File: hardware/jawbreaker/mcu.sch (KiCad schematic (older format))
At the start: 122 parts, among them J1 GSG-USB-MICRO-B, P1 ANALOG, P10 BANK1_AUX, P11 SPIFI, P12 SD, P14 LPC_ISP, P15 I2S, P16 1V8, P17 VCC, P18 CPLD_JTAG, P2 LPC_JTAG, P3 LPC_MISC, P5 GPIO, P8 BANK2_AUX, U1 GSG-IP4220CZ6, U2 LPC43XXFBD144, U3 W25Q80BV, U4 GSG-XC2C64A-7VQG100C, U5 TPS62410

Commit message: re-annotated everything
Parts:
- gave numbers to parts that had none: 26
- renumbered C24 to C125, C27 to C126, C30 to C127, C1 to C128, C2 to C129, C3 to C130, C4 to C131, C5 to C132, C7 to C133, C9 to C134, C10 to C135, C11 to C136, C12 to C137, C13 to C138, C14 to C139, C15 to C140, C17 to C141, C19 to C142, C21 to C143, C20 to C144, C28 to C145, C31 to C146, C6 to C147, C8 to C148, C22 to C149, C23 to C150, C25 to C151, C26 to C152, C29 to C153, C32 to C154, C33 to C155, C16 to C156, C18 to C159, D6 to D2, D7 to D3, D1 to D4, D2 to D5, D3 to D6, D4 to D7, D5 to D8, L1 to L10, L2 to L11, P11 to P19, P5 to P20, P1 to P21, P15 to P22, P17 to P23, P16 to P24, P14 to P25, P2 to P26, P3 to P27, P12 to P28, P18 to P29, P8 to P30, P10 to P31, R35 to R46, R37 to R47, R16 to R48, R17 to R49, R33 to R50, R32 to R51, R39 to R52, R34 to R53, R40 to R54, R36 to R55, R38 to R56, R1 to R57, R2 to R58, R28 to R59, R10 to R62, R30 to R63, R31 to R64, R11 to R65, R5 to R66, R6 to R67, R7 to R68, R14 to R69, R29 to R70, R3 to R71, R8 to R72, R9 to R73, R12 to R74, R13 to R75, R15 to R76, R18 to R77, R4 to R82, R41 to R93, R42 to R94, R43 to R95, U3 to U20, U5 to U21, U1 to U22, U2 to U23, U4 to U24

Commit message: started replacing 0603s with 0402s
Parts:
- removed C159: 47pF, symbol C
- removed R94, R95: 10k, symbol R
- C125: Description CAP CER 22PF 50V 5% NP0 0603 -> (none); Manufacturer Murata -> (none); Part Number GRM1885C1H220JA01D -> (none)
- C128, C129, C130, C131, C132, C133, C134, C135, C136, C137, C138, C139, C140, C141, C142, C144, C148, C149, C150, C151, C152, C153, C154: Description CAP CER 0.1UF 16V 10% X7R 0603 -> CAP CER 0.1UF 10V 10% X5R 0402; Part Number GRM188R71C104KA01D -> GRM155R61A104KA01D
- C147: value 4u7 -> 100nF; Description CAP CER 4.7UF 10V 10% X5R 0805 -> CAP CER 0.1UF 10V 10% X5R 0402; Manufacturer Taiyo Yuden -> Murata; Part Number LMK212BJ475KD-T -> GRM155R61A104KA01D
- C155: value 100nF -> 100pF; Description CAP CER 0.1UF 16V 10% X7R 0603 -> CAP CER 100PF 50V 5% NP0 0402; Part Number GRM188R71C104KA01D -> GRM1555C1H101JZ01D
- C156: value 100pF -> 47pF; Description CAP CER 100PF 50V 5% NP0 0603 -> CAP CER 47PF 50V 5% NP0 0402; Part Number GRM1885C1H101JA01D -> GRM1555C1H470JZ01D
- R46: Description RES 180K OHM 1/10W 1% 0603 SMD -> (none); Manufacturer Panasonic -> (none); Part Number ERJ-3EKF1803V -> (none)
- R47: Description RES 360K OHM 1/10W 1% 0603 SMD -> (none); Manufacturer Panasonic -> (none); Part Number ERJ-3EKF3603V -> (none)
- R48, R49, R51, R52, R54, R59, R60, R61, R66, R67, R68, R82, R93: Description RES 10K OHM 1/10W 5% 0603 SMD -> (none); Manufacturer Panasonic -> (none); Part Number ERJ-3GEYJ103V -> (none)
- R55: Description RES 160K OHM 1/10W 1% 0603 SMD -> (none); Manufacturer Panasonic -> (none); Part Number ERJ-3EKF1603V -> (none)
- R56: Description RES 560K OHM 1/10W 1% 0603 SMD -> (none); Manufacturer Panasonic -> (none); Part Number ERJ-3EKF5603V -> (none)
- R57, R58: Description RES 0.0 OHM 1/10W 0603 SMD -> (none); Manufacturer Panasonic -> (none); Part Number ERJ-3GEY0R00V -> (none)
- R62: Description RES 15K OHM 1/10W 5% 0603 SMD -> (none); Manufacturer Panasonic -> (none); Part Number ERJ-3GEYJ153V -> (none)
- R63, R64: value 1k8 -> 10k; Description RES 1.8K OHM 1/10W 5% 0603 SMD -> (none); Manufacturer Panasonic -> (none); Part Number ERJ-3GEYJ182V -> (none)
- R65: Description RES 33K OHM 1/10W 5% 0603 SMD -> (none); Manufacturer Panasonic -> (none); Part Number ERJ-3GEYJ333V -> (none)
- R69: Description RES 12.0K OHM 1/10W 1% 0603 SMD -> (none); Manufacturer Panasonic -> (none); Part Number ERJ-3EKF1202V -> (none)
- R70, R71, R72, R73, R74, R75, R76: Description RES 470 OHM 1/10W 5% 0603 SMD -> RES TF 1/16W 470 OHM 5% 0402; Manufacturer Panasonic -> Stackpole; Part Number ERJ-3GEYJ471V -> RMCF0402JT470R
- R83, R84, R85, R92: value DNP -> 10k; Description RES 10K OHM 1/10W 5% 0603 SMD -> (none); Manufacturer Panasonic -> (none); Part Number ERJ-3GEYJ103V -> (none)
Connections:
- net +1.8V: now also C151.1; no longer C153.1
- net BOOT0: now also R67.1; no longer R82.1
- net BOOT1: now also R68.2; no longer R93.2
- net BOOT2: now also R82.2
- net BOOT3: now also R93.2
- net DBGEN: now also R64.1; no longer R67.2
- net EN1V8: now also R76.2; no longer R76.1
- net GND: now also C156.2, R68.1, R70.1, R71.1, R82.1; no longer C155.2, R70.2, R71.2
- net GP_CLKIN: now also C155.2, C156.1; no longer C156.2
- net ISP: now also R59.1; no longer R59.2
- net LED1: now also R72.2; no longer R72.1
- net LED2: now also R73.2; no longer R73.1
- net LED3: now also R74.2; no longer R74.1
- net LPC_CLK: now also C155.1; no longer C156.1
- net RESET: now also R49.1; no longer R49.2
- net SCL: no longer R64.2
- net SDA: no longer R63.2
- net TCK: now also R66.1; no longer R68.2
- net TDO: now also R63.1; no longer R66.2
- net VBUS: no longer C148.1
- net VCC: now also C148.1, R48.2, R49.2, R59.2, R63.2, R64.2, R66.2, R67.2, R75.2; no longer C151.1, R48.1, R49.1, R59.1, R63.1, R64.1, R66.1, R67.1, R68.1, R75.1, R82.2
- net VCCIO1: now also C153.1; no longer C155.1
- net WAKEUP: now also R48.1; no longer R48.2
- net at D2.2 (K): now also R70.2; no longer R70.1
- net at D6.1 (A): now also R74.1; no longer R74.2
- net at D7.1 (A): now also R75.1; no longer R75.2
- net at D4.1 (A): now also R72.1; no longer R72.2
- net at D8.1 (A): now also R76.1; no longer R76.2
- net at D5.1 (A): now also R73.1; no longer R73.2
- net at D3.2 (K): now also R71.2; no longer R71.1

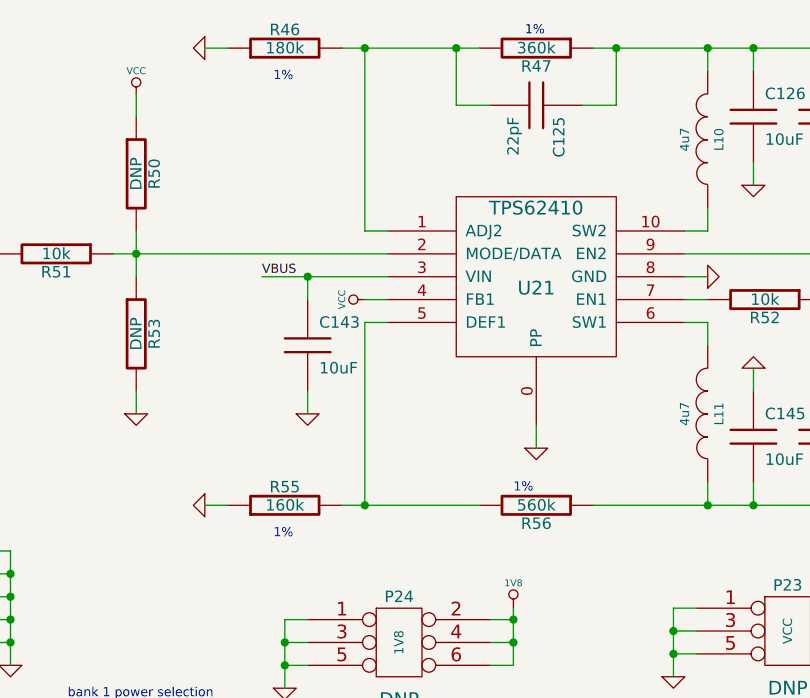
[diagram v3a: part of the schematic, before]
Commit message: updated regulator feedback resistors
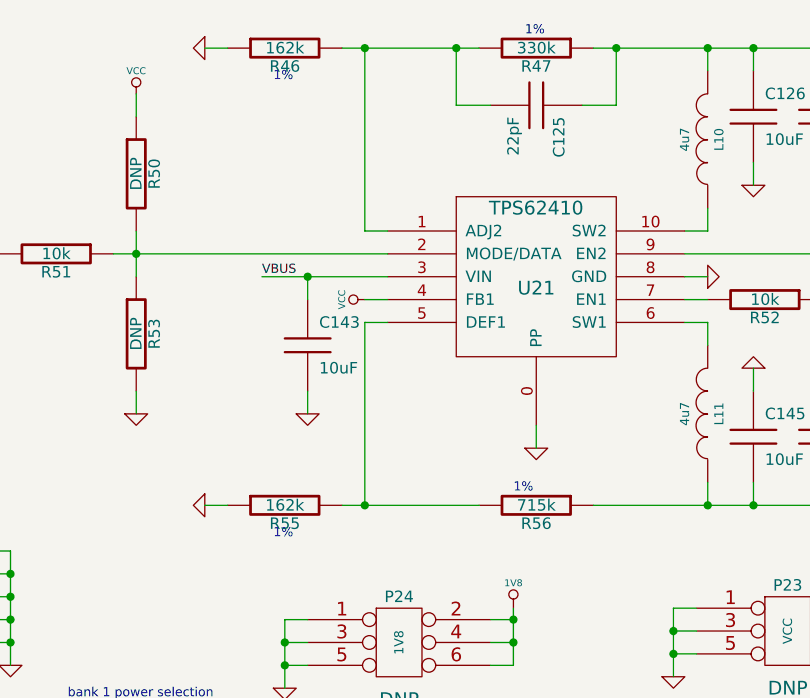
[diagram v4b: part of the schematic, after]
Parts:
- R46: value 180k -> 162k; Description (none) -> RES TF 1/16W 162K OHM 1% 0402; Manufacturer (none) -> Stackpole; Part Number (none) -> RMCF0402FT162K
- R47: value 360k -> 330k; Description (none) -> RES TF 1/16W 330K OHM 1% 0402; Manufacturer (none) -> Stackpole; Part Number (none) -> RMCF0402FT330K
- R55: value 160k -> 162k; Description (none) -> RES TF 1/16W 162K OHM 1% 0402; Manufacturer (none) -> Stackpole; Part Number (none) -> RMCF0402FT162K
- R56: value 560k -> 715k; Description (none) -> RES TF 1/16W 715K OHM 1% 0402; Manufacturer (none) -> Stackpole; Part Number (none) -> RMCF0402FT715K

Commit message: bom info
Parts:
- C125: Description (none) -> CAP CER 22PF 50V 5% NP0 0402; Manufacturer (none) -> Murata; Part Number (none) -> GRM1555C1H220JA01D
- C157, C158: Description (none) -> CAP CER 10PF 50V 5% NP0 0402; Manufacturer (none) -> Murata; Part Number (none) -> GRM1555C1H100JZ01D
- R100, R101, R102, R77, R78, R79, R80, R81, R86, R87, R88, R89, R90, R91, R96, R97, R98, R99: Description (none) -> RES 39 OHM 1/16W 5% 0402 SMD; Manufacturer (none) -> Stackpole; Part Number (none) -> RMCF0402JT39R0
- R48, R49, R51, R52, R54, R59, R60, R63, R64, R66, R67, R68, R82, R93: Description (none) -> RES 10K OHM 1/16W 5% 0402 SMD; Manufacturer (none) -> Stackpole; Part Number (none) -> RMCF0402JT10K0
- R57, R58: Description (none) -> RES 0.0 OHM 1/16W 0402 SMD; Manufacturer (none) -> Stackpole; Part Number (none) -> RMCF0402ZT0R00
- R62: Description (none) -> RES TF 1/16W 15K OHM 5% 0402; Manufacturer (none) -> Stackpole; Part Number (none) -> RMCF0402JT15K0
- R65: Description (none) -> RES TF 1/16W 33K OHM 5% 0402; Manufacturer (none) -> Stackpole; Part Number (none) -> RMCF0402JT33K0
- R69: Manufacturer (none) -> RMCF0402FT12K0; Part Number (none) -> RES TF 1/16W 12K OHM 1% 0402
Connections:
- net EN1V8: now also R54.2; no longer R54.1
- net GND: now also R54.1; no longer R54.2
- net ISP: now also R59.2; no longer R59.1
- net RESET: now also R49.2; no longer R49.1
- net TCK: now also R66.2; no longer R66.1
- net VCC: now also R48.1, R49.1, R59.1, R60.1, R66.1; no longer R48.2, R49.2, R59.2, R60.2, R66.2
- net VCCIO1: now also R60.2; no longer R60.1
- net WAKEUP: now also R48.2; no longer R48.1

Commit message: misc. corrections
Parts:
- removed R83, R84, R85, R92: 10k, symbol R
- added K? (x4): CONN_3, symbol CONN_3
- R60: value 10k -> 0; Description RES 10K OHM 1/16W 5% 0402 SMD -> (none); Manufacturer Stackpole -> (none); Note (none) -> DNP; Part Number RMCF0402JT10K0 -> (none)
- R61: value DNP -> 0
- R69: Description (none) -> RES TF 1/16W 12K OHM 1% 0402; Manufacturer RMCF0402FT12K0 -> Stackpole; Part Number RES TF 1/16W 12K OHM 1% 0402 -> RMCF0402FT12K0
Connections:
- net VCCIO1 is gone; now on net VCC: C153.1, C154.1, R60.2, R61.1, U24.38 (VCCIO1), U24.51 (VCCIO1)
- net BOOT1: now also R68.1; no longer R68.2
- net BOOT2: now also R82.1; no longer R82.2
- net BOOT3: now also R93.1; no longer R93.2
- net GND: now also R68.2, R82.2, R93.2, K?.2 (PM), K?.2 (PM), K?.2 (PM), K?.3 (P3), K?.3 (P3), K?.3 (P3), K?.3 (P3); no longer R68.1, R82.1, R93.1
- net VCC: now also K?.1 (P1), K?.1 (P1), K?.1 (P1), K?.1 (P1), K?.2 (PM)
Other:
- note added: "cut jumper traces to reconfigure"
- moved on the sheet: C155, C156, C157, C158, R60, R67, R68, R82, R93, X2

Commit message: optional RF LDO
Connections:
- net RF_LDO_ENABLE: now reaches U23.95 (P2_6)
- no-connect marks 30 -> 29
